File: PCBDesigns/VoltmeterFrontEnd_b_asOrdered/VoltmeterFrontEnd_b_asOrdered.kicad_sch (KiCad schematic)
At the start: 26 parts, among them J1 Conn_01x09_Pin, J15 V_Input, Q3 MMBT3904, Q8 AO3400A MOSFET, U10 LM4040DBZ-2.5, U7 MAX1683

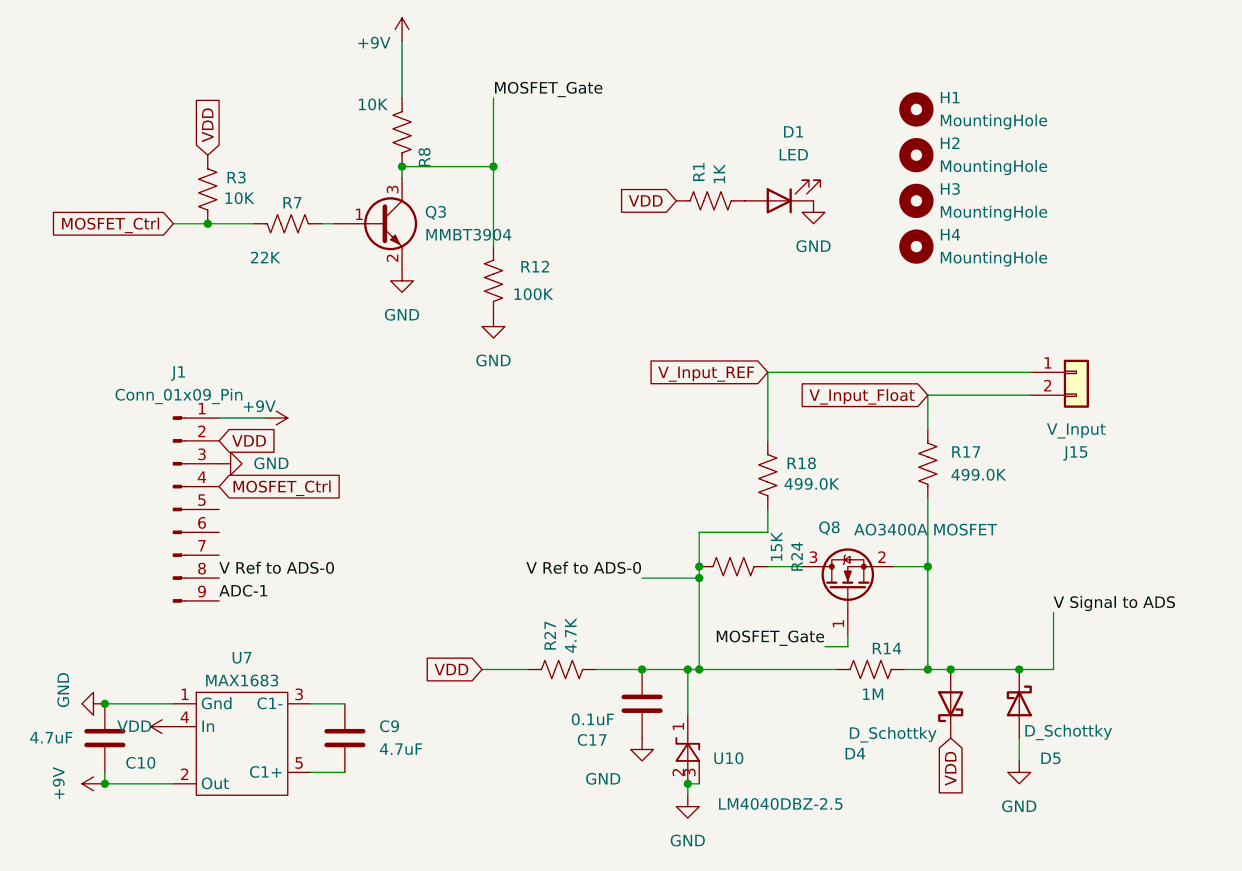
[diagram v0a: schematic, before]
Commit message: Data Capture for Open Lead Detect, Swap Differential on AdaLogger
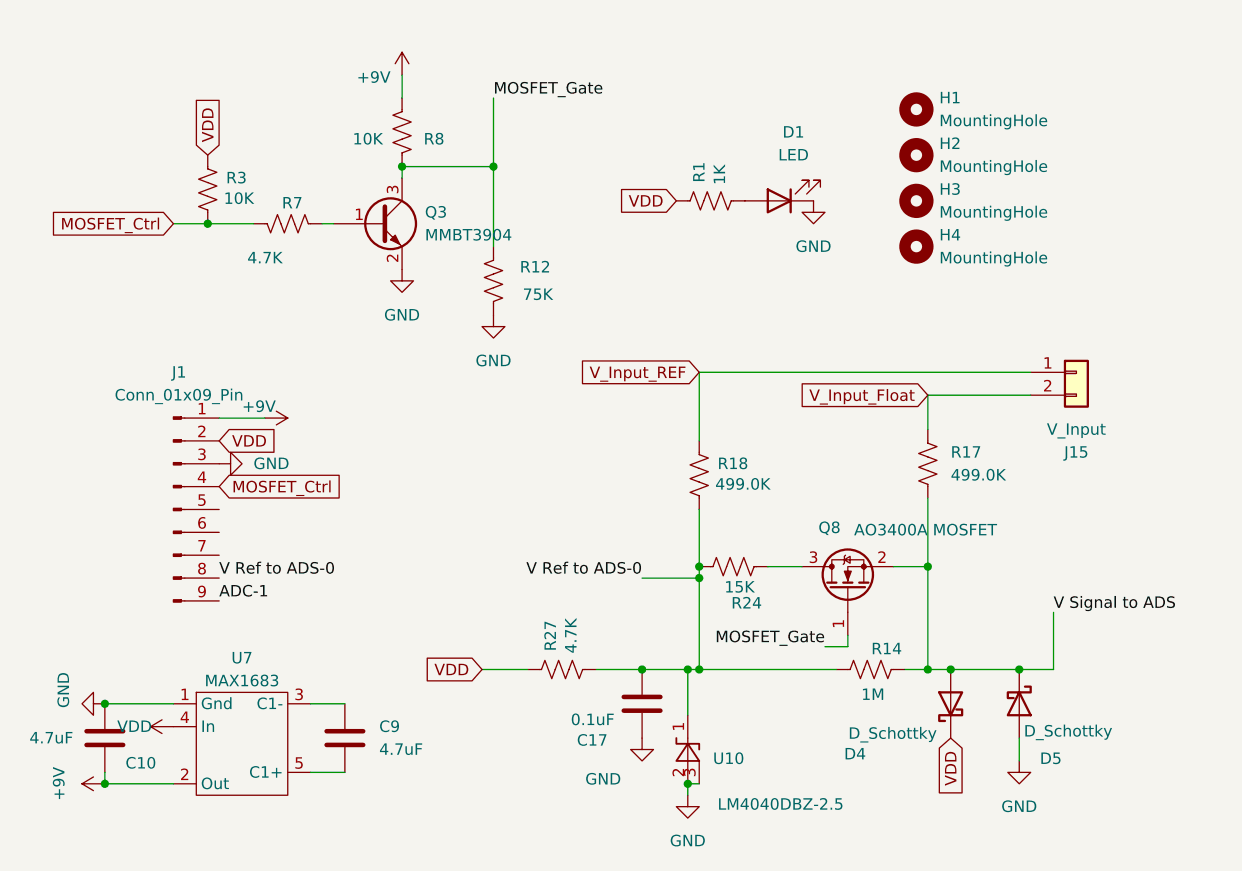
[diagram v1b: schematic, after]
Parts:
- R12: value 100K -> 75K
- R7: value 22K -> 4.7K
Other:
- moved on the sheet: R18
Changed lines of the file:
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@@
 	(wire
 		(pts
-			(xy 153.67 88.9) (xy 153.67 85.09)
+			(xy 153.67 82.55) (xy 153.67 88.9)
 		)
 		(stroke
@@
 	(wire
 		(pts
-			(xy 190.5 67.31) (xy 161.29 67.31)
+			(xy 190.5 67.31) (xy 153.67 67.31)
 		)
 		(stroke
@@
 	(wire
 		(pts
-			(xy 120.65 36.83) (xy 120.65 30.48)
+			(xy 120.65 36.83) (xy 120.65 34.29)
 		)
 		(stroke
@@
 	(wire
 		(pts
-			(xy 161.29 67.31) (xy 161.29 74.93)
+			(xy 153.67 67.31) (xy 153.67 74.93)
 		)
 		(stroke
@@
 	(wire
 		(pts
-			(xy 153.67 85.09) (xy 161.29 85.09)
-		)
-		(stroke
-			(width 0)
-			(type default)
-		)
-	)
-	(wire
-		(pts
 			(xy 175.26 88.9) (xy 179.07 88.9)
 		)
@@
 	(wire
 		(pts
-			(xy 161.29 82.55) (xy 161.29 85.09)
-		)
-		(stroke
-			(width 0)
-			(type default)
-		)
-	)
-	(wire
-		(pts
 			(xy 193.04 100.33) (xy 189.23 100.33)
 		)
@@
 	(global_label "V_Input_REF"
 		(shape input)
-		(at 161.29 67.31 180)
+		(at 153.67 67.31 180)
 		(fields_autoplaced yes)
 		(effects
@@
 		)
 		(property "Intersheetrefs" "${INTERSHEET_REFS}"
-			(at 146.9959 67.31 0)
+			(at 139.3759 67.31 0)
 			(effects
 				(font
@@
 			)
 		)
-		(property "Value" "22K"
+		(property "Value" "4.7K"
 			(at 105.41 54.61 90)
 			(effects
@@
 		(dnp no)
 		(property "Reference" "R8"
-			(at 123.19 43.434 90)
+			(at 124.206 41.402 0)
 			(effects
 				(font
@@
 		)
 		(property "Value" "10K"
-			(at 117.348 37.592 0)
+			(at 116.84 41.402 0)
 			(effects
 				(font
@@
 			)
 		)
-		(property "Value" "100K"
+		(property "Value" "75K"
 			(at 137.414 58.674 0)
 			(effects
@@
 		(dnp no)
 		(property "Reference" "R24"
-			(at 164.592 86.106 0)
+			(at 157.226 92.964 90)
 			(effects
 				(font
@@
 		)
 		(property "Value" "15K"
-			(at 162.306 85.09 0)
+			(at 156.464 91.186 90)
 			(effects
 				(font
@@
 	(symbol
 		(lib_id "Device:R_US")
-		(at 161.29 78.74 0)
+		(at 153.67 78.74 0)
 		(unit 1)
 		(exclude_from_sim no)
@@
 		(dnp no)
 		(property "Reference" "R18"
-			(at 163.322 77.47 0)
+			(at 155.702 77.47 0)
 			(effects
 				(font
@@
 		)
 		(property "Value" "499.0K"
-			(at 163.068 79.756 0)
+			(at 155.448 79.756 0)
 			(effects
 				(font
@@
 		)
 		(property "Footprint" "Resistor_SMD:R_0805_2012Metric_Pad1.20x1.40mm_HandSolder"
-			(at 162.306 78.994 90)
+			(at 154.686 78.994 90)
 			(effects
 				(font
@@
 		)
 		(property "Datasheet" "~"
-			(at 161.29 78.74 0)
+			(at 153.67 78.74 0)
 			(effects
 				(font
@@
 		)
 		(property "Description" "Resistor, US symbol"
-			(at 161.29 78.74 0)
+			(at 153.67 78.74 0)
 			(effects
 				(font
@@
 		)
 		(property "ValueTemp" ""
-			(at 161.29 78.74 0)
+			(at 153.67 78.74 0)
 			(effects
 				(font
@@
 		)
 		(property "Function" "V REF Divider"
-			(at 161.29 78.74 0)
+			(at 153.67 78.74 0)
 			(effects
 				(font
@@
 		)
 		(property "Sim.Device" ""
-			(at 161.29 78.74 0)
+			(at 153.67 78.74 0)
 			(effects
 				(font
@@
 		)
 		(property "Sim.Pins" ""
-			(at 161.29 78.74 0)
+			(at 153.67 78.74 0)
 			(effects
 				(font
@@
 	(symbol
 		(lib_id "power:+9V")
-		(at 120.65 30.48 0)
+		(at 120.65 34.29 0)
 		(mirror y)
 		(unit 1)
@@
 		(dnp no)
 		(property "Reference" "#PWR050"
-			(at 120.65 34.29 0)
+			(at 120.65 38.1 0)
 			(effects
 				(font
@@
 		)
 		(property "Value" "+9V"
-			(at 119.38 30.734 0)
+			(at 119.38 34.544 0)
 			(effects
 				(font
@@
 		)
 		(property "Footprint" ""
-			(at 120.65 30.48 0)
+			(at 120.65 34.29 0)
 			(effects
 				(font
@@
 		)
 		(property "Datasheet" ""
-			(at 120.65 30.48 0)
+			(at 120.65 34.29 0)
 			(effects
 				(font
@@
 		)
 		(property "Description" "Power symbol creates a global label with name \"+9V\""
-			(at 120.65 30.48 0)
+			(at 120.65 34.29 0)
 			(effects
 				(font
